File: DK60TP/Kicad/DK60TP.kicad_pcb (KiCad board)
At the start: 2 copper layers, 285 x 94.5 mm, 193 parts, among them J1 USB_mini_micro_B, K1 K00, K10 K11, K11 K21, K12 K31, K13 K41, K14 K41, K15 K02, K16 K12, K17 K22, K18 K32, K19 K42, K2 K10, K20 K42, K21 K03, K22 K13, K23 K23, K24 K33, K27 K04, K28 K14, K29 K24, K3 K20, K30 K34, K32 K05, K33 K15, K34 K25, K35 K35, K38 K06, K39 K16, K4 K20, K40 K26, K41 K36, K42 K46, K43 K46, K44 K46, K45 K46, K46 K07, K47 K17, K48 K27, K49 K37, K5 K30, K50 K08, K51 K18, K52 K28, K53 K38, K54 K09, K55 K19, K56 K29, K57 K39, K58 K49, K59 K0A, K6 K30, K60 K1A, K61 K2A, K62 K3A, K63 K4A, K64 K4A, K65 K0B, K66 K1B, K67 K2B, K68 K3B, K69 K4B, K7 K40, K70 K4B, K71 K4B, K72 K0C, K73 K1C, K74 K2C, K75 K3C, K76 K4C, K77 K4C, K78 K0D, K79 K0D, K8 K40, K80 K1D, K81 K2D, K82 K1D, K83 K3D, K84 K3C, K85 K4D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

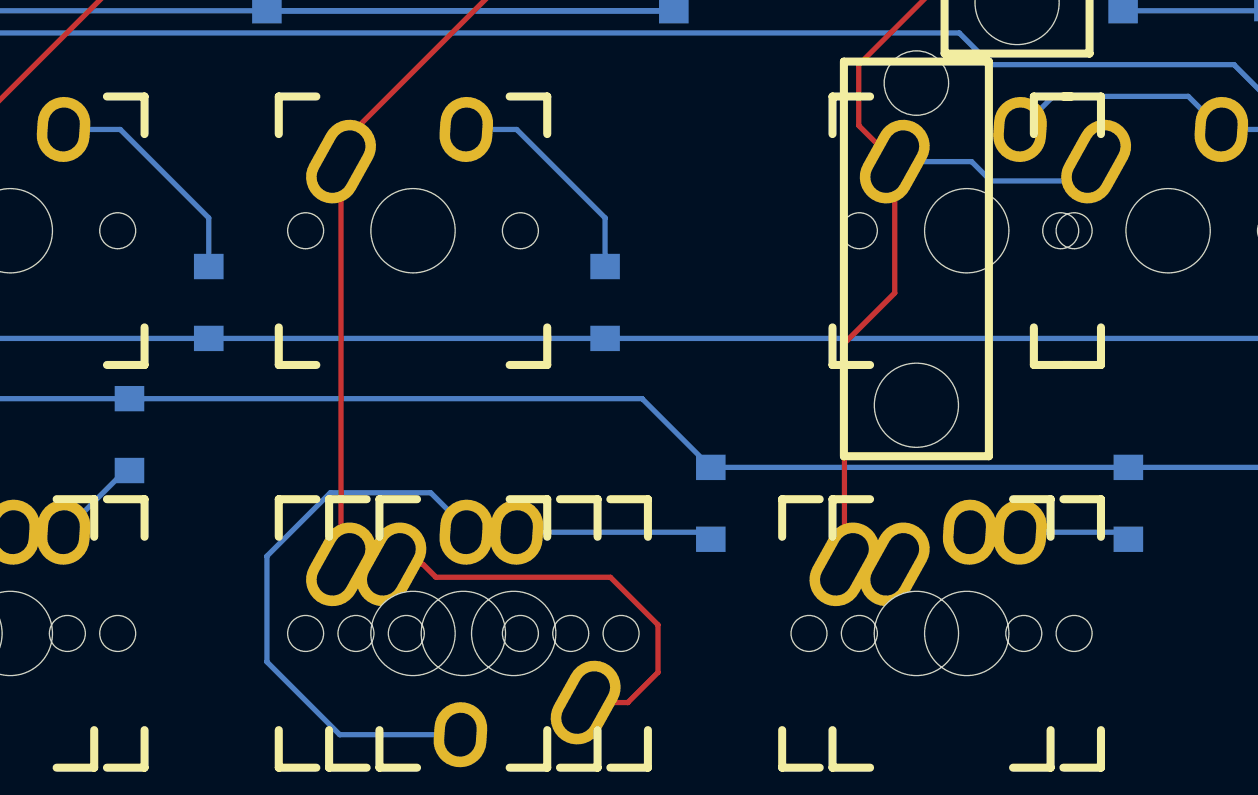
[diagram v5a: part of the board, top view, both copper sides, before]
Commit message: - Moved back logo
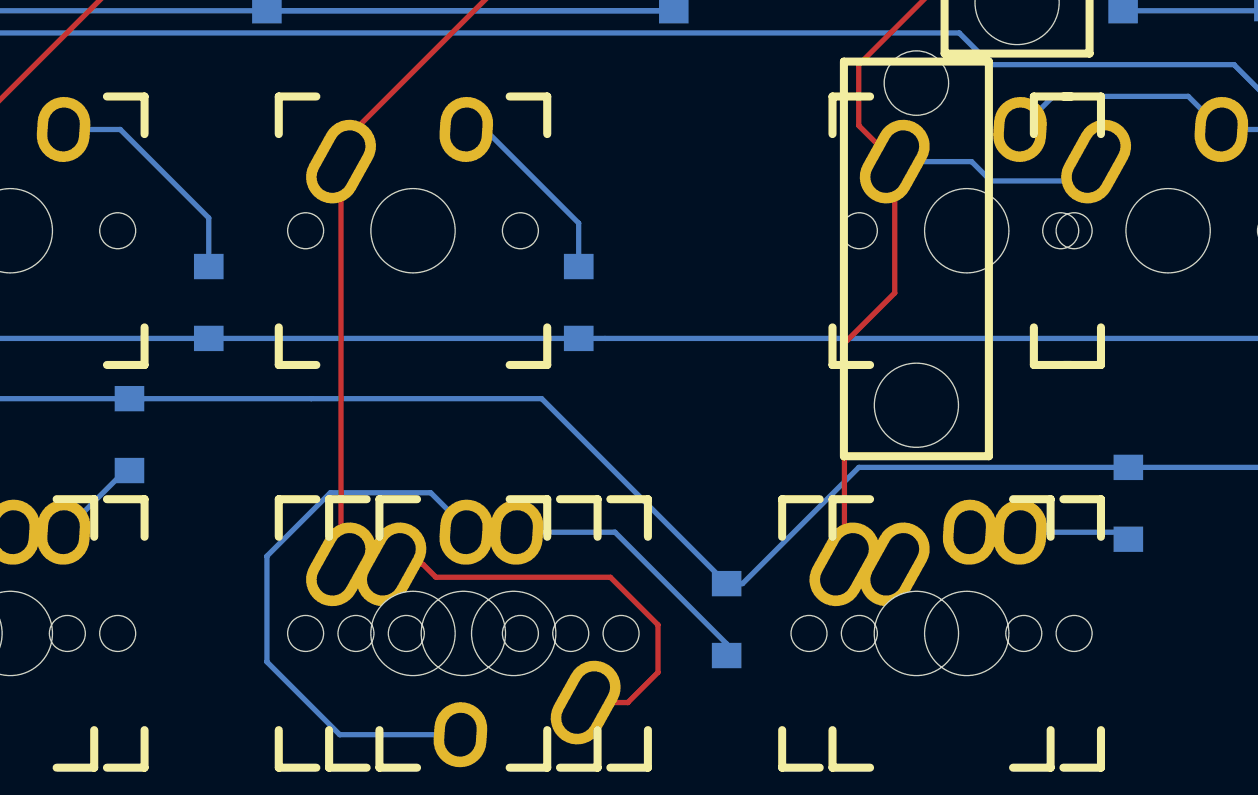
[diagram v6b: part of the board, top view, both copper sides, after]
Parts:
- moved D58 5.55 mm to (267.2, 106.5)
- moved D57 1.25 mm to (260.2, 91.5)
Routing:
- net /Row4: track 358.5 -> 363.0 mm
- net Net-(D58-Pad2): track 38.8 -> 42.2 mm
- net Net-(D57-Pad2): track 10.6 -> 9.20 mm
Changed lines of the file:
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@@
   (general
     (links 290)
-    (no_connects 0)
+    (no_connects 1)
     (area 28.924999 21.824999 314.075001 116.475001)
     (thickness 1.6)
     (drawings 42)
-    (tracks 1078)
+    (tracks 1082)
     (zones 0)
     (modules 193)
@@
   )
   (module Footprint:D_SOD123 (layer B.Cu)
-    (at 261.5 91.5 90)
+    (at 260.25 91.5 90)
     (attr smd)
     (fp_text reference D57 (at 0 -1.925 90) (layer B.SilkS) hide
@@
   )
   (module Footprint:D_SOD123 (layer B.Cu)
-    (at 266.5 101 270)
+    (at 267.25 106.5 270)
     (attr smd)
     (fp_text reference D58 (at 0 -1.925 270) (layer B.SilkS) hide
@@
   (segment (start 232.635 101.5) (end 233.50125 102.36625) (width 0.25) (layer B.Cu) (net 58) (status 30))
   (segment (start 233.50125 102.36625) (end 235.8825 102.36625) (width 0.25) (layer B.Cu) (net 58) (status 30))
+  (segment (start 247.6 96.05) (end 258.5 96.05) (width 0.25) (layer B.Cu) (net 59))
+  (segment (start 258.5 96.05) (end 267.25 104.8) (width 0.25) (layer B.Cu) (net 59) (status 800000))
+  (segment (start 267.25 104.8) (end 268 104.8) (width 0.25) (layer B.Cu) (net 59) (status 400000))
+  (segment (start 268 104.8) (end 273.5 99.3) (width 0.25) (layer B.Cu) (net 59))
+  (segment (start 273.5 99.3) (end 286.25 99.3) (width 0.25) (layer B.Cu) (net 59) (status 800000))
   (segment (start 307.5 53.5) (end 307.5 47.5) (width 0.25) (layer B.Cu) (net 59))
   (segment (start 307.5 47.5) (end 302.25 42.25) (width 0.25) (layer B.Cu) (net 59))
@@
   (segment (start 221.45 96.05) (end 206.04 111.46) (width 0.25) (layer B.Cu) (net 59))
   (segment (start 206.04 111.46) (end 202.9 111.46) (width 0.25) (layer B.Cu) (net 59) (status 20))
-  (segment (start 239 96.05) (end 263.25 96.05) (width 0.25) (layer B.Cu) (net 59) (status 10))
-  (segment (start 263.25 96.05) (end 266.5 99.3) (width 0.25) (layer B.Cu) (net 59) (status 20))
+  (segment (start 239 96.05) (end 247.6 96.05) (width 0.25) (layer B.Cu) (net 59) (status 10))
   (segment (start 310.5 66.25) (end 302 74.75) (width 0.25) (layer B.Cu) (net 59))
   (segment (start 302 92.75) (end 304.5 95.25) (width 0.25) (layer B.Cu) (net 59))
@@
   (segment (start 310.5 56.5) (end 310.5 66.25) (width 0.25) (layer B.Cu) (net 59))
   (segment (start 307.5 53.5) (end 310.5 56.5) (width 0.25) (layer B.Cu) (net 59))
-  (segment (start 286.25 99.3) (end 266.5 99.3) (width 0.25) (layer B.Cu) (net 59) (status 30))
   (segment (start 75 110.7) (end 76.75 108.95) (width 0.25) (layer B.Cu) (net 59) (status 20))
   (segment (start 76.75 108.95) (end 76.95 108.95) (width 0.25) (layer B.Cu) (net 59) (status 30))
@@
   (segment (start 264.4575 64.26625) (end 264.4575 74.0075) (width 0.25) (layer B.Cu) (net 62) (status 30))
   (segment (start 264.4575 74.0075) (end 264.75 74.3) (width 0.25) (layer B.Cu) (net 62) (status 30))
-  (segment (start 254.9325 83.31625) (end 257.31625 83.31625) (width 0.25) (layer B.Cu) (net 63) (status 10))
-  (segment (start 261.5 87.5) (end 261.5 89.8) (width 0.25) (layer B.Cu) (net 63) (status 20))
-  (segment (start 257.31625 83.31625) (end 261.5 87.5) (width 0.25) (layer B.Cu) (net 63))
+  (segment (start 254.9325 83.31625) (end 255.81625 83.31625) (width 0.25) (layer B.Cu) (net 63))
+  (segment (start 255.81625 83.31625) (end 260.25 87.75) (width 0.25) (layer B.Cu) (net 63))
+  (segment (start 260.25 87.75) (end 260.25 89.8) (width 0.25) (layer B.Cu) (net 63))
+  (segment (start 257.31375 102.36625) (end 261.96625 102.36625) (width 0.25) (layer B.Cu) (net 64) (status 400000))
+  (segment (start 261.96625 102.36625) (end 267.25 107.65) (width 0.25) (layer B.Cu) (net 64) (status 800000))
+  (segment (start 267.25 107.65) (end 267.25 108.2) (width 0.25) (layer B.Cu) (net 64) (status C00000))
   (segment (start 254.9325 102.36625) (end 254.9325 102.1825) (width 0.25) (layer B.Cu) (net 64) (status 30))
   (segment (start 254.9325 102.1825) (end 253.25 100.5) (width 0.25) (layer B.Cu) (net 64) (status 10))
@@
   (segment (start 248.5 100.5) (end 245.5 103.5) (width 0.25) (layer B.Cu) (net 64))
   (segment (start 253.25 100.5) (end 248.5 100.5) (width 0.25) (layer B.Cu) (net 64))
-  (segment (start 257.31375 102.36625) (end 266.16625 102.36625) (width 0.25) (layer B.Cu) (net 64) (status 30))
-  (segment (start 266.16625 102.36625) (end 266.5 102.7) (width 0.25) (layer B.Cu) (net 64) (status 30))
   (segment (start 254.9325 102.36625) (end 257.31375 102.36625) (width 0.25) (layer F.Cu) (net 64) (status 30))
   (segment (start 269.22 26.16625) (end 269.22 36.27) (width 0.25) (layer B.Cu) (net 65) (status 30))

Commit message: - Added libraries/footprint from mohitg11 (TS65) - Added Backlit for DK60TP (need to fix bug for bottom row)
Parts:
- added C10: 10uF, Capacitors_SMD:C_0805_HandSoldering, B.Cu at (213.4, 104.1)
- added C11: 10uF, Capacitors_SMD:C_0805_HandSoldering, B.Cu at (210.8, 106.7)
- added D100: LED, Footprint:LED_TH_BIVAR, F.Cu at (261.9, 74.1)
- added D101: LED, Footprint:LED_TH_BIVAR, F.Cu at (42.9, 112.2)
- added D102: LED, Footprint:LED_TH_BIVAR, F.Cu at (147.6, 74.1)
- added D103: LED, Footprint:LED_TH_BIVAR, F.Cu at (40.5, 112.2)
- added D104: LED, Footprint:LED_TH_BIVAR, F.Cu at (71.4, 74.1)
- added D105: LED, Footprint:LED_TH_BIVAR, F.Cu at (45.6, 74.1)
- added D106: LED, Footprint:LED_TH_BIVAR, F.Cu at (40.5, 74.1)
- added D107: LED, Footprint:LED_TH_BIVAR, F.Cu at (42.9, 55.1)
- added D108: LED, Footprint:LED_TH_BIVAR, F.Cu at (66.7, 55.1)
- added D109: LED, Footprint:LED_TH_BIVAR, F.Cu at (85.7, 55.1)
- added D110: LED, Footprint:LED_TH_BIVAR, F.Cu at (104.8, 55.1)
- added D111: LED, Footprint:LED_TH_BIVAR, F.Cu at (123.8, 55.1)
- added D112: LED, Footprint:LED_TH_BIVAR, F.Cu at (142.9, 55.1)
- added D113: LED, Footprint:LED_TH_BIVAR, F.Cu at (161.9, 55.1)
- added D114: LED, Footprint:LED_TH_BIVAR, F.Cu at (40.5, 93.2)
- added D115: LED, Footprint:LED_TH_BIVAR, F.Cu at (38.1, 36.0)
- added D116: LED, Footprint:LED_TH_BIVAR, F.Cu at (76.2, 36.0)
- added D117: LED, Footprint:LED_TH_BIVAR, F.Cu at (114.3, 36.0)
- added D118: LED, Footprint:LED_TH_BIVAR, F.Cu at (152.4, 36.0)
- added D119: LED, Footprint:LED_TH_BIVAR, F.Cu at (171.4, 36.0)
- added D120: LED, Footprint:LED_TH_BIVAR, F.Cu at (181.0, 55.1)
- added D121: LED, Footprint:LED_TH_BIVAR, F.Cu at (190.5, 36.0)
- added D122: LED, Footprint:LED_TH_BIVAR, F.Cu at (209.6, 36.0)
- added D123: LED, Footprint:LED_TH_BIVAR, F.Cu at (200.0, 55.1)
- added D124: LED, Footprint:LED_TH_BIVAR, F.Cu at (228.6, 36.0)
- added D125: LED, Footprint:LED_TH_BIVAR, F.Cu at (133.3, 36.0)
- added D126: LED, Footprint:LED_TH_BIVAR, F.Cu at (266.7, 36.0)
- added D127: LED, Footprint:LED_TH_BIVAR, F.Cu at (285.8, 36.0)
- added D128: LED, Footprint:LED_TH_BIVAR, F.Cu at (295.9, 36.0)
- added D129: LED, Footprint:LED_TH_BIVAR, F.Cu at (57.1, 36.0)
- added D130: LED, Footprint:LED_TH_BIVAR, F.Cu at (95.2, 36.0)
- added D131: LED, Footprint:LED_TH_BIVAR, F.Cu at (304.8, 36.0)
- added D132: LED, Footprint:LED_TH_BIVAR, F.Cu at (219.1, 55.1)
- added D133: LED, Footprint:LED_TH_BIVAR, F.Cu at (238.1, 55.1)
- added D134: LED, Footprint:LED_TH_BIVAR, F.Cu at (257.2, 55.1)
- added D135: LED, Footprint:LED_TH_BIVAR, F.Cu at (276.2, 55.1)
- added D136: LED, Footprint:LED_TH_BIVAR, F.Cu at (300.0, 44.9)
- added D137: LED, Footprint:LED_TH_BIVAR, F.Cu at (297.7, 59.5)
- added D138: LED, Footprint:LED_TH_BIVAR, F.Cu at (247.7, 36.0)
- added D139: LED, Footprint:LED_TH_BIVAR, F.Cu at (292.9, 74.1)
- added D140: LED, Footprint:LED_TH_BIVAR, F.Cu at (256.5, 120.7)
- added D141: LED, Footprint:LED_TH_BIVAR, F.Cu at (233.4, 112.2)
- added D142: LED, Footprint:LED_TH_BIVAR, F.Cu at (231.0, 112.2)
- added D143: LED, Footprint:LED_TH_BIVAR, F.Cu at (251.5, 120.7)
- added D144: LED, Footprint:LED_TH_BIVAR, F.Cu at (246.4, 120.7)
- added D145: LED, Footprint:LED_TH_BIVAR, F.Cu at (288.1, 93.2)
- added D20: LED, Footprint:LED_TH_BIVAR, F.Cu at (252.4, 93.2)
- added D25: LED, Footprint:LED_TH_BIVAR, F.Cu at (278.6, 93.2)
- added D30: LED, Footprint:LED_TH_BIVAR, F.Cu at (304.8, 93.2)
- added D69: LED, Footprint:LED_TH_BIVAR, F.Cu at (300.0, 112.2)
- added D70: LED, Footprint:LED_TH_BIVAR, F.Cu at (276.2, 112.2)
- added D71: LED, Footprint:LED_TH_BIVAR, F.Cu at (233.4, 93.2)
- added D72: LED, Footprint:LED_TH_BIVAR, F.Cu at (176.2, 93.2)
- added D73: LED, Footprint:LED_TH_BIVAR, F.Cu at (185.7, 74.1)
- added D74: LED, Footprint:LED_TH_BIVAR, F.Cu at (204.8, 74.1)
- added D75: LED, Footprint:LED_TH_BIVAR, F.Cu at (242.9, 74.1)
- added D76: LED, Footprint:LED_TH_BIVAR, F.Cu at (281.0, 74.1)
- added D77: LED, Footprint:LED_TH_BIVAR, F.Cu at (128.6, 74.1)
- added D78: LED, Footprint:LED_TH_BIVAR, F.Cu at (138.1, 93.2)
- added D79: LED, Footprint:LED_TH_BIVAR, F.Cu at (119.1, 93.2)
- added D80: LED, Footprint:LED_TH_BIVAR, F.Cu at (109.5, 74.1)
- added D81: LED, Footprint:LED_TH_BIVAR, F.Cu at (100.0, 93.2)
- added D82: LED, Footprint:LED_TH_BIVAR, F.Cu at (87.9, 112.2)
- added D83: LED, Footprint:LED_TH_BIVAR, F.Cu at (90.5, 112.2)
- added D84: LED, Footprint:LED_TH_BIVAR, F.Cu at (302.4, 112.2)
- added D85: LED, Footprint:LED_TH_BIVAR, F.Cu at (195.3, 93.2)
- added D86: LED, Footprint:LED_TH_BIVAR, F.Cu at (278.6, 112.2)
- added D87: LED, Footprint:LED_TH_BIVAR, F.Cu at (90.5, 74.1)
- added D88: LED, Footprint:LED_TH_BIVAR, F.Cu at (214.3, 93.2)
- added D89: LED, Footprint:LED_TH_BIVAR, F.Cu at (81.0, 93.2)
- added D90: LED, Footprint:LED_TH_BIVAR, F.Cu at (61.9, 93.2)
- added D91: LED, Footprint:LED_TH_BIVAR, F.Cu at (157.2, 93.2)
- added D92: LED, Footprint:LED_TH_BIVAR, F.Cu at (171.4, 112.2)
- added D93: LED, Footprint:LED_TH_BIVAR, F.Cu at (159.5, 112.2)
- added D94: LED, Footprint:LED_TH_BIVAR, F.Cu at (152.4, 112.2)
- added D95: LED, Footprint:LED_TH_BIVAR, F.Cu at (166.7, 74.1)
- added D96: LED, Footprint:LED_TH_BIVAR, F.Cu at (223.8, 74.1)
- added D97: LED, Footprint:LED_TH_BIVAR, F.Cu at (50.0, 93.2)
- added D98: LED, Footprint:LED_TH_BIVAR, F.Cu at (66.7, 112.2)
- added D99: LED, Footprint:LED_TH_BIVAR, F.Cu at (64.3, 112.2)
- added L1: 4.7uH, Footprint:Inductor_Bourn_4mmx4mm, B.Cu at (222.2, 100.3)
- added R5: R, Resistors_SMD:R_0805_HandSoldering, B.Cu at (215.9, 101.6)
- added U1: PAM2804, Footprint:SOT-23-5, B.Cu at (214.2, 97.0)
- moved D48 9.37 mm to (311.5, 36.5)
- moved D1 8.71 mm to (34.0, 43.5), turned to 135 degrees
- moved D31 8.68 mm to (163.5, 39.8)
- moved D13 8.49 mm to (101.5, 76.4)
- moved D19 8.28 mm to (110.0, 91.0)
- moved D26 8.19 mm to (144.0, 39.8)
- moved D46 8.00 mm to (234.5, 76.0)
- moved D16 7.95 mm to (105.5, 39.8)
- moved D42 7.75 mm to (215.2, 76.0)
- moved D40 7.70 mm to (200.8, 39.8)
- moved D14 7.50 mm to (91.0, 95.2)
- moved D64 7.50 mm to (290.5, 42.5), turned to 0 degrees
- moved D11 7.46 mm to (86.2, 39.8)
- moved D21 7.46 mm to (124.2, 39.8)
- moved D36 7.46 mm to (181.2, 39.8)
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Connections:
- U0 pad 12: /Col5 -> BACKLIT
- U0 pad 8: Net-(U0-Pad8) -> /ColD
- U0 pad 9: /ColD -> /Col5
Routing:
- net LED_AN: track 0.00 -> 1728.4 mm, vias 0 -> 28
- net LED_CATH: track 0.00 -> 1700.2 mm, vias 0 -> 32
- net BACKLIT: track 0.00 -> 88.2 mm, vias 0 -> 4
- net GND: track 170.1 -> 217.9 mm, vias 10 -> 20
- net /Row0: track 457.9 -> 414.7 mm
- net VCC: track 477.7 -> 515.8 mm, vias 4 -> 6
- net /Row1: track 386.6 -> 349.4 mm
- net /ColD: track 309.4 -> 343.2 mm
- net Net-(D64-Pad2): track 21.4 -> 53.3 mm
- net /Col9: track 274.4 -> 290.9 mm, vias 2 -> 5
- net /Row3: track 264.5 -> 281.0 mm, vias 0 -> 5
- net /Row2: track 295.8 -> 280.3 mm
- net D5: track 87.3 -> 74.4 mm, vias 2 -> 3
- net /Col5: track 183.6 -> 196.4 mm
- net /Row4: track 363.0 -> 375.3 mm, vias 2 -> 6
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
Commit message: - Updated README - Added Cherry's footprints - Removed ALPS compatibity for DK60TP
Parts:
- removed K43: K46, Footprint:Mx_Alps_100
- K1, K10, K11, K12, K14, K15, K16, K17, K18, K21, K22, K23, K24, K27, K28, K29, K30, K32, K33, K34, K35, K38, K39, K40, K41, K46, K47, K48, K49, K50, K51, K52, K53, K54, K55, K56, K57, K58, K59, K60, K61, K62, K65, K66, K67, K68, K69, K72, K73, K74, K76, K78, K83, K9: footprint Footprint:Mx_Alps_100 -> Footprint:Mx_100
- K13, K19, K6, K63, K7, K70, K77, K85: footprint Footprint:Mx_Alps_125 -> Footprint:Mx_125
- K2, K20, K64, K71, K8, K80, K86: footprint Footprint:Mx_Alps_150 -> Footprint:Mx_150
- K3, K84: footprint Footprint:Mx_Alps_175 -> Footprint:Mx_175
- K4: footprint Footprint:Mx_Alps_175_STEPPED -> Footprint:Mx_175_STEPPED
- K42: footprint Footprint:Mx_Alps_600 -> Footprint:Mx_600
- K44: footprint Footprint:Mx_Alps_625 -> Footprint:Mx_625
- K45: footprint Footprint:Mx_Alps_700 -> Footprint:Mx_700
- K5, K81: footprint Footprint:Mx_Alps_225 -> Footprint:Mx_225
- K75: footprint Footprint:Mx_Alps_275 -> Footprint:Mx_275
- K79, K82: footprint Footprint:Mx_Alps_200 -> Footprint:Mx_200
- moved D144 10.2 mm to (252.1, 112.2), turned to 180 degrees
- moved D143 8.99 mm to (254.6, 112.2)
- moved D140 8.44 mm to (257.2, 112.2), turned to 180 degrees
- moved K42 0.33 mm to (171.1, 107.2)
- turned K69 to 0 degrees
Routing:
- net GND: track 217.9 -> 246.3 mm, vias 20 -> 25
- net Net-(D58-Pad2): track 42.2 -> 17.4 mm
- net LED_CATH: track 1700.2 -> 1677.4 mm, vias 32 -> 30
- net /ColB: track 275.2 -> 258.4 mm
- net LED_AN: track 1728.4 -> 1714.8 mm
- net Net-(D35-Pad2): track 34.0 -> 38.5 mm
- net /CAPS_LED: track 105.7 -> 107.8 mm
- net /Row0: track 414.7 -> 416.6 mm
- net /Col9: track 290.9 -> 289.1 mm
- net /Col5: track 196.4 -> 194.8 mm
- net /Col6: track 145.2 -> 144.0 mm
- net Net-(D62-Pad2): track 23.5 -> 24.4 mm
- net /Col7: track 146.6 -> 145.9 mm
